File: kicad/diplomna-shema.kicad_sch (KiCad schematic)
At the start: 24 parts, among them J1 Power input 12VDC, J2 To Load cell, J3 To Load cell, J4 To Load cell, J5 Load cell, J7 micro switch, M1 Stepper_Motor_bipolar, M2 Motor_Servo, U1 TCS3200, U2 TCRT5000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

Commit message: Add files via upload
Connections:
- net +3.3V: no longer R6.2, U4.7 (PIN_7)
- net at R5.2, U4.13 (PIN_13), U4.9 (PIN_9): no longer U4.10 (PIN_10)
- new net: R6.2, U4.10 (PIN_10), U4.7 (PIN_7)
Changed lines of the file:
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@@
   (junction (at 54.61 54.61) (diameter 0) (color 0 0 0 0)
   )
-  (junction (at 130.81 152.4) (diameter 0) (color 0 0 0 0)
-  )
   (junction (at 125.73 139.7) (diameter 0) (color 0 0 0 0)
   )
   (junction (at 100.33 25.4) (diameter 0) (color 0 0 0 0)
   )
-  (junction (at 128.27 152.4) (diameter 0) (color 0 0 0 0)
+  (junction (at 133.35 152.4) (diameter 0) (color 0 0 0 0)
   )
   (junction (at 100.33 49.53) (diameter 0) (color 0 0 0 0)
   )
   (junction (at 74.93 109.22) (diameter 0) (color 0 0 0 0)
-  )
-  (junction (at 133.35 152.4) (diameter 0) (color 0 0 0 0)
   )
   (junction (at 128.27 151.13) (diameter 0) (color 0 0 0 0)
@@
     (stroke (width 0) (type default) (color 0 0 0 0))
   )
-  (wire (pts (xy 130.81 152.4) (xy 133.35 152.4))
-    (stroke (width 0) (type default) (color 0 0 0 0))
-  )
   (wire (pts (xy 95.25 133.35) (xy 97.79 133.35))
     (stroke (width 0) (type default) (color 0 0 0 0))
@@
     (stroke (width 0) (type default) (color 0 0 0 0))
   )
+  (wire (pts (xy 123.19 152.4) (xy 133.35 152.4))
+    (stroke (width 0) (type default) (color 0 0 0 0))
+  )
   (wire (pts (xy 101.6 100.33) (xy 109.22 100.33))
     (stroke (width 0) (type default) (color 0 0 0 0))
@@
     (stroke (width 0) (type default) (color 0 0 0 0))
   )
-  (wire (pts (xy 123.19 152.4) (xy 128.27 152.4))
-    (stroke (width 0) (type default) (color 0 0 0 0))
-  )

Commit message: Add files via upload
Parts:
- added R9: 10kΩ, Resistor_SMD:R_0805_2012Metric, symbol Device:R
- renumbered R4 to R9
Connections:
- net GND: now also R9.1
- net at A2.39, J7.2 (Pin_2): no longer R9.1
- net at A2.49: now also R9.1; no longer U4.11 (PIN_11)
- new net: R9.2, U4.11 (PIN_11)
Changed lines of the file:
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@@
 (kicad_sch (version 20211123) (generator eeschema)
   (paper "A4")
-  (junction (at 74.93 116.84) (diameter 0) (color 0 0 0 0)
-  )
   (junction (at 54.61 54.61) (diameter 0) (color 0 0 0 0)
   )
@@
     (stroke (width 0) (type default) (color 0 0 0 0))
   )
-  (wire (pts (xy 115.57 176.53) (xy 115.57 125.73))
+  (wire (pts (xy 115.57 176.53) (xy 115.57 137.16))
     (stroke (width 0) (type default) (color 0 0 0 0))
   )
@@
     (stroke (width 0) (type default) (color 0 0 0 0))
   )
-  (wire (pts (xy 72.39 111.76) (xy 72.39 116.84))
+  (wire (pts (xy 72.39 111.76) (xy 72.39 120.65))
     (stroke (width 0) (type default) (color 0 0 0 0))
   )
@@
     (stroke (width 0) (type default) (color 0 0 0 0))
   )
-  (wire (pts (xy 90.17 119.38) (xy 90.17 113.03))
+  (wire (pts (xy 115.57 129.54) (xy 115.57 125.73))
+    (stroke (width 0) (type default) (color 0 0 0 0))
+  )
+  (wire (pts (xy 90.17 120.65) (xy 90.17 113.03))
     (stroke (width 0) (type default) (color 0 0 0 0))
   )
@@
     (stroke (width 0) (type default) (color 0 0 0 0))
   )
-  (wire (pts (xy 74.93 116.84) (xy 74.93 119.38))
-    (stroke (width 0) (type default) (color 0 0 0 0))
-  )
   (wire (pts (xy 163.83 128.27) (xy 171.45 128.27))
     (stroke (width 0) (type default) (color 0 0 0 0))
   )
   (wire (pts (xy 193.04 105.41) (xy 193.04 107.95))
-    (stroke (width 0) (type default) (color 0 0 0 0))
-  )
-  (wire (pts (xy 72.39 116.84) (xy 74.93 116.84))
     (stroke (width 0) (type default) (color 0 0 0 0))
   )
@@
     (stroke (width 0) (type default) (color 0 0 0 0))
   )
-  (wire (pts (xy 74.93 119.38) (xy 90.17 119.38))
+  (wire (pts (xy 72.39 120.65) (xy 90.17 120.65))
     (stroke (width 0) (type default) (color 0 0 0 0))
   )
@@
     (pin "1")
   )
+  (symbol (lib_id "Device:R") (at 115.57 133.35 0) (unit 1)
+    (in_bom yes) (on_board yes)
+    (property "Reference" "R9" (id 0) (at 113.03 133.35 90)
+      (effects (font (size 1.27 1.27)) (justify right))
+    )
+    (property "Value" "10kΩ" (id 1) (at 115.57 130.81 90)
+      (effects (font (size 1.27 1.27)) (justify right))
+    )
+    (property "Footprint" "Resistor_SMD:R_0805_2012Metric" (id 2) (at 113.792 133.35 90)
+      (effects (font (size 1.27 1.27)) hide)
+    )
+    (property "Datasheet" "~" (id 3) (at 115.57 133.35 0)
+      (effects (font (size 1.27 1.27)) hide)
+    )
+    (pin "1")
+    (pin "2")
+  )
   (symbol (lib_id "power:+5V") (at 123.19 90.17 90) (unit 1)
     (in_bom yes) (on_board yes) (fields_autoplaced)
@@
   (symbol (lib_id "Device:R") (at 74.93 113.03 180) (unit 1)
     (in_bom yes) (on_board yes) (fields_autoplaced)
-    (property "Reference" "R4" (id 0) (at 77.47 111.7599 0)
+    (property "Reference" "R9" (id 0) (at 77.47 111.7599 0)
       (effects (font (size 1.27 1.27)) (justify right))
     )
@@
     (pin "3")
   )
+  (symbol (lib_id "power:GND") (at 74.93 116.84 0) (unit 1)
+    (in_bom yes) (on_board yes) (fields_autoplaced)
+    (property "Reference" "#PWR?" (id 0) (at 74.93 123.19 0)
+      (effects (font (size 1.27 1.27)) hide)
+    )
+    (property "Value" "GND" (id 1) (at 77.47 118.1099 0)
+      (effects (font (size 1.27 1.27)) (justify left))
+    )
+    (property "Footprint" "" (id 2) (at 74.93 116.84 0)
+      (effects (font (size 1.27 1.27)) hide)
+    )
+    (property "Datasheet" "" (id 3) (at 74.93 116.84 0)
+      (effects (font (size 1.27 1.27)) hide)
+    )
+    (pin "1")
+  )
   (symbol (lib_id "power:GND") (at 233.68 86.36 90) (unit 1)
     (in_bom yes) (on_board yes) (fields_autoplaced)
@@
       (reference "#PWR0134") (unit 1) (value "GND") (footprint "")
     )
+    (path "/b468b5ea-be41-4ee0-ae2b-75b06b92833b"
+      (reference "#PWR?") (unit 1) (value "GND") (footprint "")
+    )
     (path "/bd7465b6-a0ee-4899-a936-92210c87b969"
       (reference "A1") (unit 1) (value "A4988") (footprint "Module:Pololu_Breakout-16_15.2x20.3mm")
@@
       (reference "R3") (unit 1) (value "10kΩ") (footprint "Resistor_SMD:R_0805_2012Metric")
     )
-    (path "/743b64d3-3793-42c4-8ef5-369420bbce01"
-      (reference "R4") (unit 1) (value "10kΩ") (footprint "Resistor_SMD:R_0805_2012Metric")
-    )
     (path "/9b5ab66b-863d-4300-96a7-77f06099b210"
       (reference "R5") (unit 1) (value "10kΩ") (footprint "Resistor_SMD:R_0805_2012Metric")
@@
       (reference "R8") (unit 1) (value "10kΩ") (footprint "Resistor_SMD:R_0805_2012Metric")
     )
+    (path "/71abb4cb-79ca-4729-9735-f351c6542bb5"
+      (reference "R9") (unit 1) (value "10kΩ") (footprint "Resistor_SMD:R_0805_2012Metric")
+    )
+    (path "/743b64d3-3793-42c4-8ef5-369420bbce01"
+      (reference "R9") (unit 1) (value "10kΩ") (footprint "Resistor_SMD:R_0805_2012Metric")
+    )
     (path "/993ddd06-1faf-4930-adc0-702aaa5d5bfd"

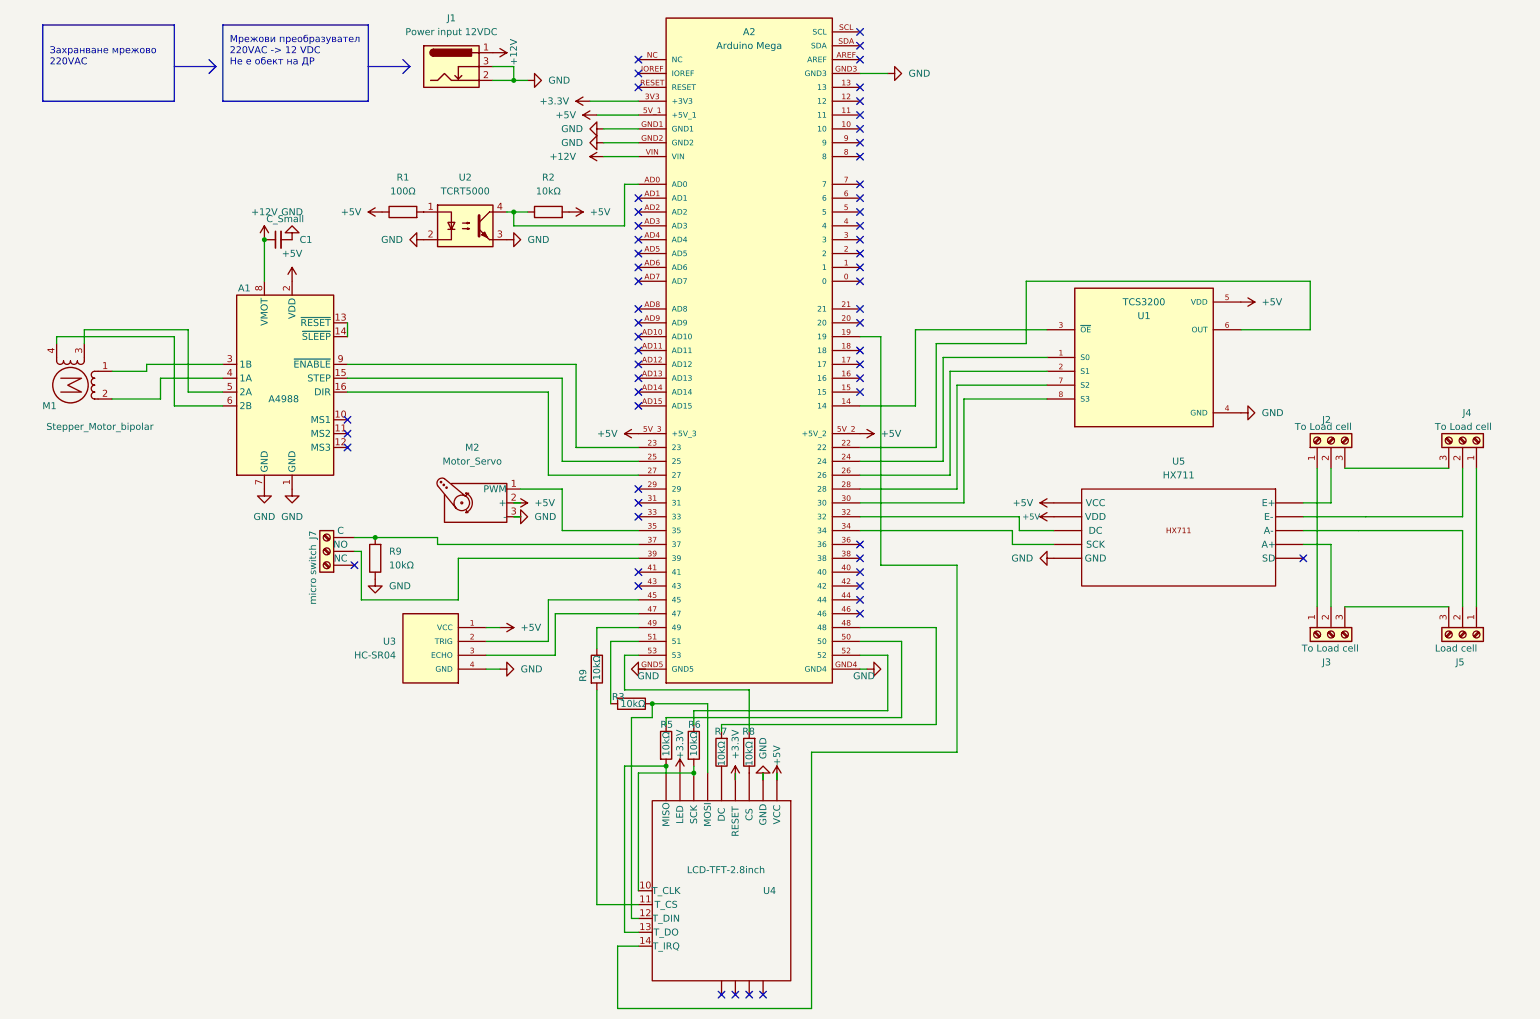
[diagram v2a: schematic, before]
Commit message: последна версия - корекции по платка и схема, нови 3Dчасти за конструкция със сменен мотор и преправен код
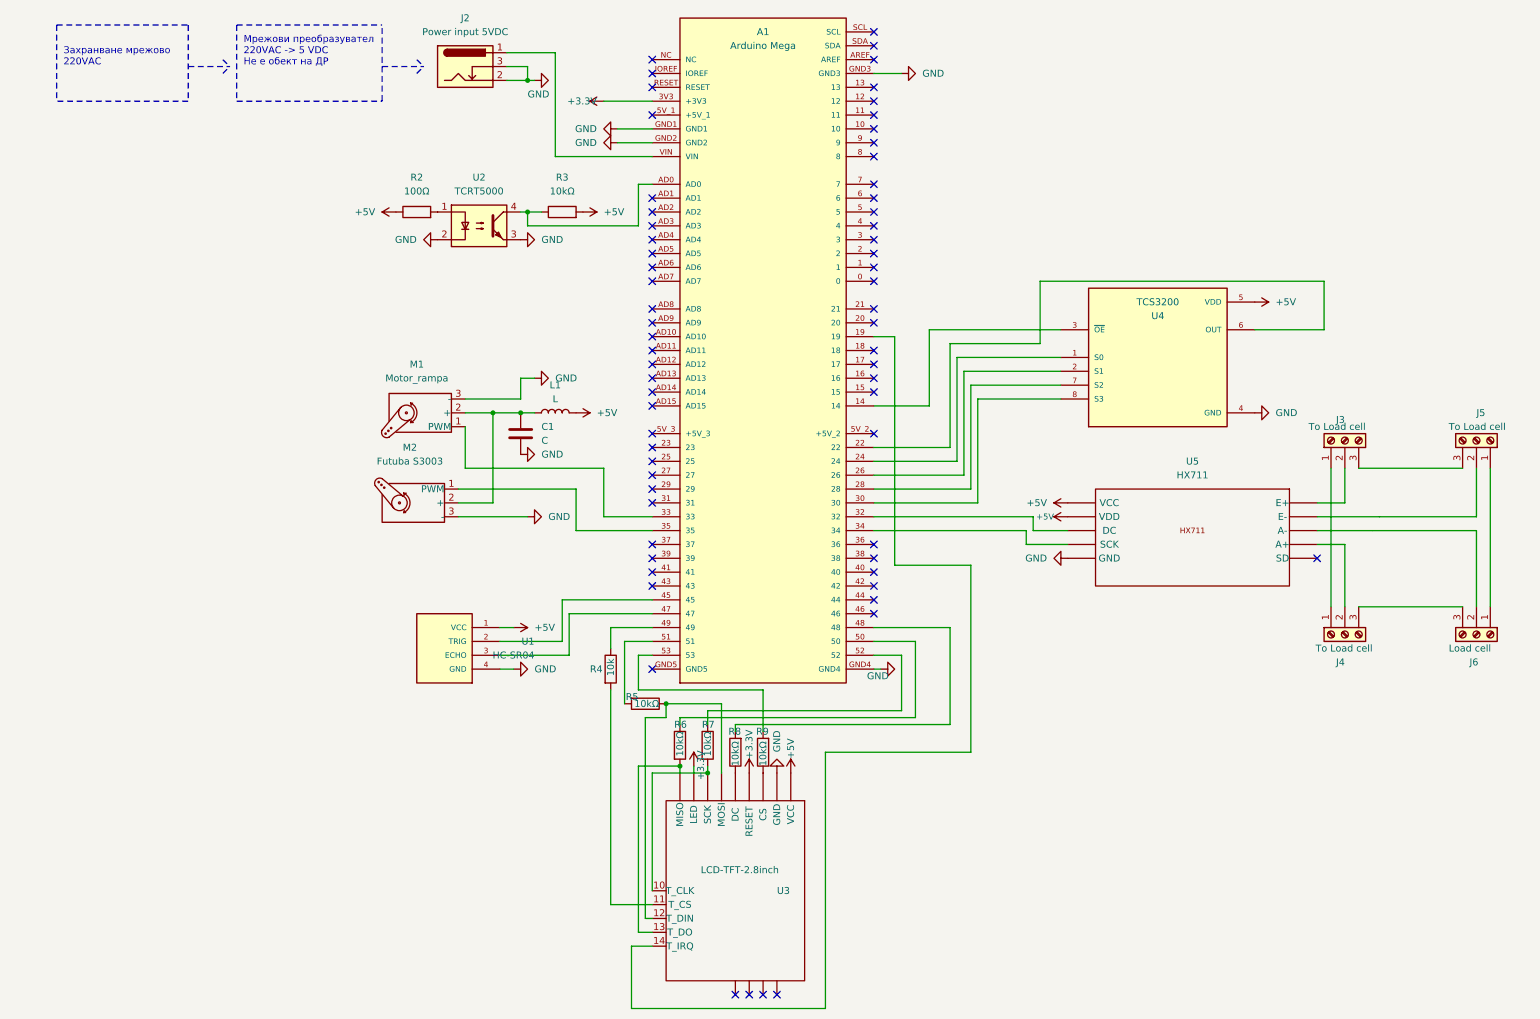
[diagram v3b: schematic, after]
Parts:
- removed A1: A4988, Module:Pololu_Breakout-16_15.2x20.3mm, symbol Driver_Motor:Pololu_Breakout_A4988
- removed A2: Arduino Mega, Library:arduino_mega2560, symbol A000067:A000067
- removed C1: C_Small, Capacitor_SMD:CP_Elec_4x3, symbol Device:C_Small
- removed J1: Power input 12VDC, Connector_BarrelJack:BarrelJack_GCT_DCJ200-10-A_Horizontal, symbol Connector:Barrel_Jack_Switch
- removed J2: To Load cell, TerminalBlock_Phoenix:TerminalBlock_Phoenix_MPT-0,5-3-2.54_1x03_P2.54mm_Horizontal, symbol Connector:Screw_Terminal_01x03
- removed J7: micro switch, TerminalBlock_Phoenix:TerminalBlock_Phoenix_MPT-0,5-3-2.54_1x03_P2.54mm_Horizontal, symbol Connector:Screw_Terminal_01x03
- removed M1: Stepper_Motor_bipolar, Connector_PinHeader_2.54mm:PinHeader_1x01_P2.54mm_Vertical, symbol Motor:Stepper_Motor_bipolar
- removed R1: 100Ω, Resistor_SMD:R_0805_2012Metric, symbol Device:R
- removed R9 (x2): 10kΩ, Resistor_SMD:R_0805_2012Metric, symbol Device:R
- removed U1: TCS3200, Library:TCS3200 color sensor, symbol TCS3200:TCS3200
- removed U3: HC-SR04, HC-SR04:XCVR_HC-SR04, symbol HC-SR04:HC-SR04
- removed U4: LCD-TFT-2.8inch, Library:2.8inch_tft-lcd, symbol tft-lcd:LCD-TFT-2.8inch
- added A1: Arduino Mega, Library:arduino_mega2560, symbol A000067:A000067
- added C1: C, Capacitor_SMD:CP_Elec_8x5.4, symbol Device:C
- added J2: Power input 5VDC, Connector_BarrelJack:BarrelJack_GCT_DCJ200-10-A_Horizontal, symbol Connector:Barrel_Jack_Switch
- added J6: Load cell, TerminalBlock_Phoenix:TerminalBlock_Phoenix_MPT-0,5-3-2.54_1x03_P2.54mm_Horizontal, symbol Connector:Screw_Terminal_01x03
- added L1: L, Inductor_SMD:L_Coilcraft_LPS5030, symbol Device:L
- added M1: Motor_rampa, Connector_PinHeader_2.54mm:PinHeader_1x03_P2.54mm_Vertical, symbol Motor:Motor_Servo
- added R4: 10k, Resistor_SMD:R_0805_2012Metric, symbol Device:R
- added R9: 10kΩ, Resistor_SMD:R_0805_2012Metric, symbol Device:R
- added U1: HC-SR04, Library:XCVR_HC-SR04, symbol HC-SR04:HC-SR04
- added U3: LCD-TFT-2.8inch, Library:2.8inch_tft-lcd, symbol tft-lcd:LCD-TFT-2.8inch
- added U4: TCS3200, Library:TCS3200 color sensor, symbol TCS3200:TCS3200
- J5: value Load cell -> To Load cell
- M2: value Motor_Servo -> Futuba S3003
- R2: value 10kΩ -> 100Ω
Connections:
- net +3.3V: now also A1.3V3 (+3V3), U3.4 (PIN_4), U3.8 (PIN_8)
- net +5V: now also R2.1, R3.2, L1.2, U1.1 (VCC), U3.1 (PIN_1), U4.5 (VDD); no longer M2.2 (+), R2.2
- net GND: now also A1.GND1, A1.GND2, A1.GND3, A1.GND4, C1.2, J2.2, J2.3, M1.3 (-), U1.4 (GND), U3.2 (PIN_2), U4.4 (GND)
- net at R6.1: now also A1.50
- net at R6.2: now also U3.13 (PIN_13), U3.9 (PIN_9)
- net at U5.8 (PIN_8): now also A1.32
- net at U5.9 (PIN_9): now also A1.34
- net at M2.1 (PWM): now also A1.35
- net at R7.2: now also U3.10 (PIN_10), U3.7 (PIN_7)
- net at R5.1: now also U3.12 (PIN_12), U3.6 (PIN_6)
- net at R8.2: now also A1.48
- net at U2.4: now also R3.1, A1.AD0; no longer R2.1
- net at U5.1 (PIN_1): now also J3.2 (Pin_2)
- net at J4.2 (Pin_2): now also U5.4 (PIN_4); no longer U5.2 (PIN_2)
- net at U5.3 (PIN_3): now also J6.2 (Pin_2); no longer J5.2 (Pin_2)
- net at U2.1: now also R2.2
- net at J4.1 (Pin_1): now also J3.1 (Pin_1); no longer J5.1 (Pin_1)
- net at R5.2: now also A1.51
- net at R8.1: now also U3.5 (PIN_5)
- net at R7.1: now also A1.52
- net at J4.3 (Pin_3): now also J6.3 (Pin_3)
- new net: R4.2, U3.11 (PIN_11)
- new net: A1.19, U3.14 (PIN_14)
- new net: R9.1, U3.3 (PIN_3)
- new net: A1.49, R4.1
- new net: C1.1, L1.1, M1.2 (+), M2.2 (+)
- new net: A1.14, U4.3 (~{OE})
- new net: A1.22, U4.6 (OUT)
- new net: A1.24, U4.1 (S0)
- new net: A1.26, U4.2 (S1)
- new net: A1.28, U4.7 (S2)
- new net: A1.30, U4.8 (S3)
- new net: A1.33, M1.1 (PWM)
- new net: A1.45, U1.2 (TRIG)
- new net: A1.47, U1.3 (ECHO)
- new net: A1.53, R9.2
- new net: A1.VIN, J2.1
- new net: J5.1 (Pin_1), J6.1 (Pin_1)
- new net: J5.2 (Pin_2), U5.2 (PIN_2)
- no-connect marks 61 -> 65
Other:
- note added: "Мрежови преобразувател 220VAC -> 5 VDC Не е обект на ДР"
- note removed: "Мрежови преобразувател 220VAC -> 12 VDC Не е обект на ДР"
